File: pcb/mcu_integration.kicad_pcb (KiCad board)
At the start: 4 copper layers, 90.2 x 95.9 mm, 83 parts, among them IC1 TL7660IDGKR, IC10 AD844_OPAMP_MEL, IC3 FOD814_OPTO_NOSHD, IC5 FOD814_OPTO_MEL, IC6 AD844_OPAMP_AL, IC7 FOD814_OPTO_AL, IC8 AD844_OPAMP_NOSHD, J4 Conn_01x02, J5 DM3BT-DSF-PEJS, M1 MountingHole_Pad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

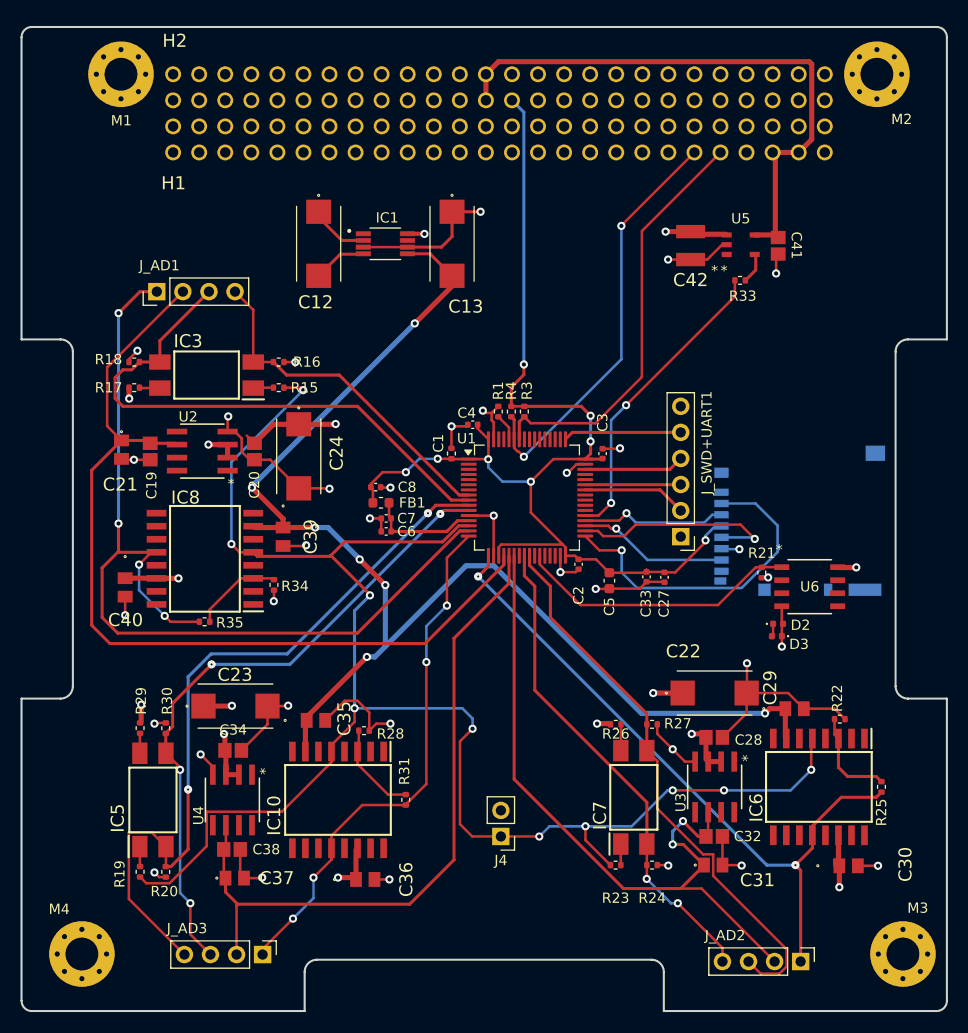
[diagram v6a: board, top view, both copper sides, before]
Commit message: Added RC Ladder Circuit
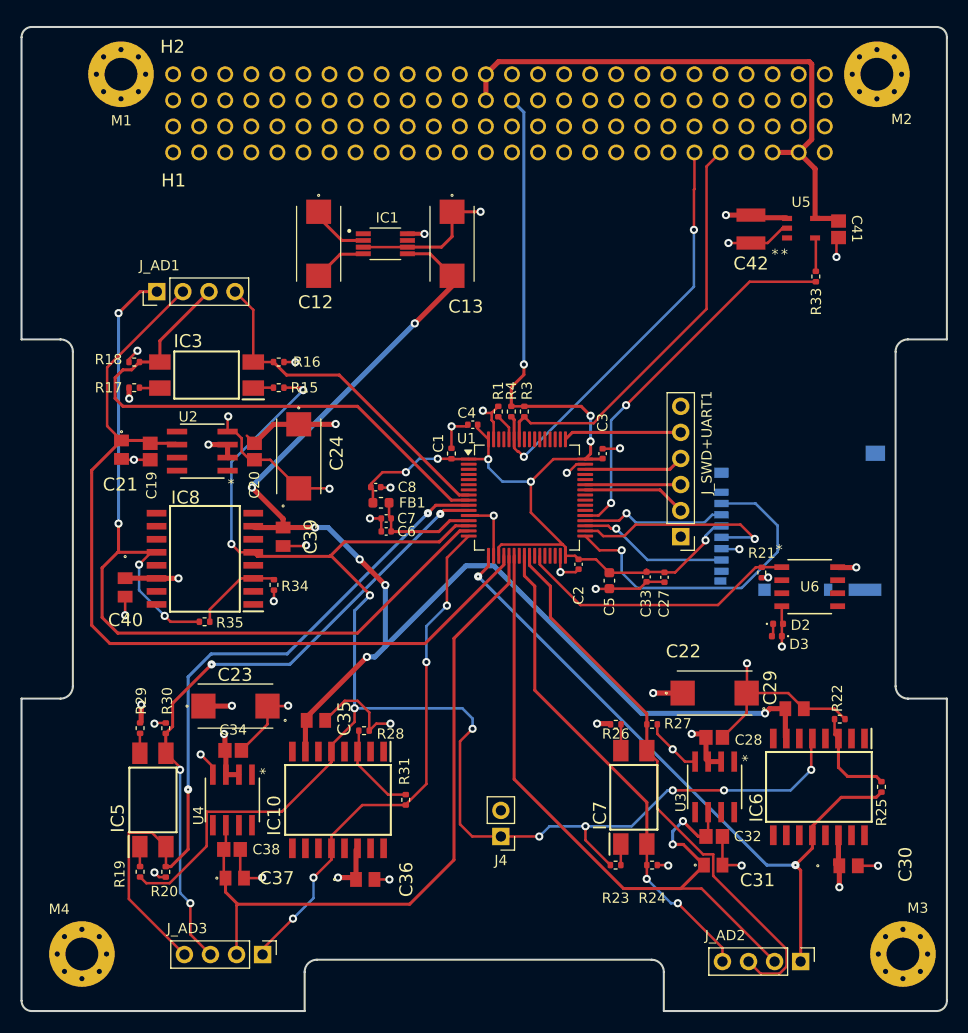
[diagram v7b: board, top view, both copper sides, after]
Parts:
- moved R33 7.39 mm to (169.9, 75.9), turned to 90 degrees
- moved C42 6.10 mm to (163.6, 71.3)
- moved C41 6.10 mm to (172.2, 71.3)
- moved U5 6.10 mm to (168.5, 71.2)
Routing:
- net MOSFET_CONTROL: track 29.7 -> 36.6 mm
- net +5V_EXT: track 57.1 -> 56.5 mm

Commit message: Routed all RC ladder connections
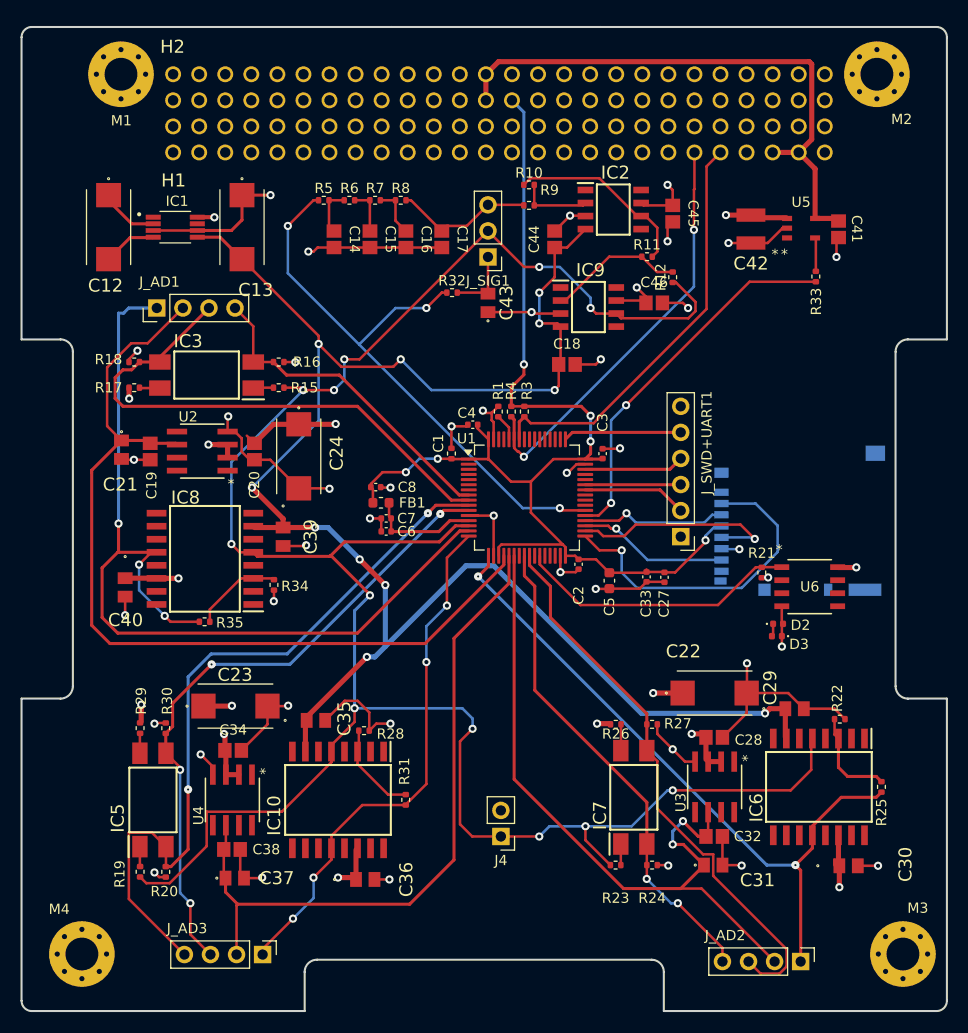
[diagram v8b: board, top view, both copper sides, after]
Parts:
- added C14: 0.1u, capstone:CAPC220145_88N_KEM-0.1u, F.Cu at (123.0, 72.3)
- added C15: 0.1u, capstone:CAPC220145_88N_KEM-0.1u, F.Cu at (126.5, 72.3)
- added C16: 0.1u, capstone:CAPC220145_88N_KEM-0.1u, F.Cu at (130.0, 72.3)
- added C17: 0.1u, capstone:CAPC220145_88N_KEM-0.1u, F.Cu at (133.5, 72.3)
- added C18: 0.1u, capstone:CAPC220145_88N_KEM-0.1u, F.Cu at (145.7, 84.5)
- added C43: 0.01u, capstone:C0805, F.Cu at (138.0, 78.5)
- added C44: 0.1u, capstone:CAPC220145_88N_KEM-0.1u, F.Cu at (144.5, 72.3)
- added C45: 0.1u, capstone:CAPC220145_88N_KEM-0.1u, F.Cu at (156.0, 69.8)
- added C46: 0.1u, capstone:CAPC220145_88N_KEM-0.1u, F.Cu at (154.2, 78.5)
- added IC2: TL081IDT, capstone:SOIC127P600X175-8N, F.Cu at (150.2, 69.4)
- added IC9: TL081IDT, capstone:SOIC127P600X175-8N, F.Cu at (147.8, 78.9)
- added J_SIG1: Conn_01x03, Connector_PinHeader_2.54mm:PinHeader_1x03_P2.54mm_Vertical, F.Cu at (138.0, 74.0)
- added R10: 15K, Resistor_SMD:R_0402_1005Metric, F.Cu at (142.0, 67.0)
- added R11: 10K, Resistor_SMD:R_0402_1005Metric, F.Cu at (153.5, 74.0)
- added R12: 10K, Resistor_SMD:R_0402_1005Metric, F.Cu at (156.0, 76.0)
- added R32: 56k, Resistor_SMD:R_0402_1005Metric, F.Cu at (134.5, 77.5)
- added R5: 100K, Resistor_SMD:R_0402_1005Metric, F.Cu at (122.0, 68.5)
- added R6: 100K, Resistor_SMD:R_0402_1005Metric, F.Cu at (124.5, 68.5)
- added R7: 100K, Resistor_SMD:R_0402_1005Metric, F.Cu at (127.0, 68.5)
- added R8: 100K, Resistor_SMD:R_0402_1005Metric, F.Cu at (129.5, 68.5)
- added R9: 10K, Resistor_SMD:R_0402_1005Metric, F.Cu at (142.0, 69.0)
- moved C12 20.5 mm to (101.0, 71.1)
- moved C13 20.5 mm to (114.0, 71.1)
- moved IC1 20.5 mm to (107.5, 71.1)
- moved J_AD1 1.60 mm to (105.7, 79.0)
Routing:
- net SIG_SQUARE: track 0.00 -> 57.8 mm, vias 0 -> 3
- net ADC1_IN0_SINE: track 161.8 -> 215.9 mm, vias 10 -> 12
- net -5V Output: track 125.6 -> 172.0 mm, vias 7 -> 11
- net GND: track 152.1 -> 183.5 mm, vias 35 -> 41
- net INVERT_SINE: track 0.00 -> 18.7 mm
- net RC_OUTPUT: track 0.00 -> 13.8 mm
- net Net-(IC9-INVERTING_INPUT): track 0.00 -> 13.3 mm
- net +5V: track 60.7 -> 70.9 mm, vias 15 -> 17
- net Net-(IC2-INVERTING_INPUT): track 0.00 -> 7.09 mm
- net Net-(J_SIG1-Pin_1): track 0.00 -> 6.61 mm
- net Net-(C16-Pad1): track 0.00 -> 4.90 mm
- net Net-(C14-Pad1): track 0.00 -> 4.68 mm
- net Net-(C15-Pad1): track 0.00 -> 4.48 mm
- net ADC1_IN10_OPTO_F_NOSHD: track 34.0 -> 32.4 mm
- net ADC1_IN11_OPTO_E_NOSHD: track 54.4 -> 52.8 mm
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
